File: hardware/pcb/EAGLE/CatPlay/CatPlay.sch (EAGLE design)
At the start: 5 parts

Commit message: updated pcb and gitignore
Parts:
- added Q1: 2N7002, CatPlay:2N7002
- added R1: (no value), rcl:R-US_R0603
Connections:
- new net N$1: Q1.D, R1.1
- net 5V: now also R1.2
- net L+: now also Q1.S
- net LSR: now also Q1.G
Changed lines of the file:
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@@
 <layers>
 <layer number="1" name="Top" color="4" fill="1" visible="no" active="no"/>
+<layer number="2" name="Route2" color="16" fill="1" visible="no" active="no"/>
+<layer number="3" name="Route3" color="17" fill="1" visible="no" active="no"/>
+<layer number="4" name="Route4" color="18" fill="1" visible="no" active="no"/>
+<layer number="5" name="Route5" color="19" fill="1" visible="no" active="no"/>
+<layer number="6" name="Route6" color="25" fill="1" visible="no" active="no"/>
+<layer number="7" name="Route7" color="26" fill="1" visible="no" active="no"/>
+<layer number="8" name="Route8" color="27" fill="1" visible="no" active="no"/>
+<layer number="9" name="Route9" color="28" fill="1" visible="no" active="no"/>
+<layer number="10" name="Route10" color="29" fill="1" visible="no" active="no"/>
+<layer number="11" name="Route11" color="30" fill="1" visible="no" active="no"/>
+<layer number="12" name="Route12" color="20" fill="1" visible="no" active="no"/>
+<layer number="13" name="Route13" color="21" fill="1" visible="no" active="no"/>
+<layer number="14" name="Route14" color="22" fill="1" visible="no" active="no"/>
+<layer number="15" name="Route15" color="23" fill="1" visible="no" active="no"/>
 <layer number="16" name="Bottom" color="1" fill="1" visible="no" active="no"/>
 <layer number="17" name="Pads" color="2" fill="1" visible="no" active="no"/>
@@
 <part name="GND3" library="supply1" library_urn="urn:adsk.eagle:library:371" deviceset="GND" device=""/>
 <part name="GND4" library="supply1" library_urn="urn:adsk.eagle:library:371" deviceset="GND" device=""/>
+<part name="Q1" library="CatPlay" deviceset="2N7002" device=""/>
+<part name="R1" library="rcl" library_urn="urn:adsk.eagle:library:334" deviceset="R-US_" device="R0603" package3d_urn="urn:adsk.eagle:package:23555/3"/>
 </parts>
 <sheets>
@@
 <attribute name="VALUE" x="27.94" y="35.56" size="1.778" layer="96"/>
 </instance>
+<instance part="Q1" gate="G$1" x="35.56" y="-17.78" smashed="yes">
+<attribute name="VALUE" x="24.13" y="-17.78" size="1.778" layer="96"/>
+<attribute name="NAME" x="24.13" y="-15.24" size="1.778" layer="95"/>
+</instance>
+<instance part="R1" gate="G$1" x="38.1" y="-2.54" smashed="yes" rot="R90">
+<attribute name="NAME" x="36.6014" y="-6.35" size="1.778" layer="95" rot="R90"/>
+<attribute name="VALUE" x="41.402" y="-6.35" size="1.778" layer="96" rot="R90"/>
+</instance>
 </instances>
 <busses>
@@
 <label x="-10.16" y="-7.62" size="1.27" layer="95" xref="yes"/>
 </segment>
+<segment>
+<pinref part="Q1" gate="G$1" pin="S"/>
+<wire x1="38.1" y1="-22.86" x2="38.1" y2="-25.4" width="0.1524" layer="91"/>
+<wire x1="38.1" y1="-25.4" x2="43.18" y2="-25.4" width="0.1524" layer="91"/>
+<label x="43.18" y="-25.4" size="1.27" layer="95" xref="yes"/>
+</segment>
 </net>
 <net name="5V" class="0">
@@
 <wire x1="38.1" y1="48.26" x2="25.4" y2="48.26" width="0.1524" layer="91"/>
 <label x="25.4" y="48.26" size="1.27" layer="95" rot="R180" xref="yes"/>
+</segment>
+<segment>
+<pinref part="R1" gate="G$1" pin="2"/>
+<wire x1="38.1" y1="2.54" x2="38.1" y2="5.08" width="0.1524" layer="91"/>
+<wire x1="38.1" y1="5.08" x2="27.94" y2="5.08" width="0.1524" layer="91"/>
+<label x="27.94" y="5.08" size="1.27" layer="95" rot="R180" xref="yes"/>
 </segment>
 </net>
@@
 <wire x1="30.48" y1="17.78" x2="25.4" y2="17.78" width="0.1524" layer="91"/>
 <label x="25.4" y="17.78" size="1.27" layer="95" rot="R180" xref="yes"/>
+</segment>
+<segment>
+<pinref part="Q1" gate="G$1" pin="G"/>
+<wire x1="33.02" y1="-20.32" x2="27.94" y2="-20.32" width="0.1524" layer="91"/>
+<label x="27.94" y="-20.32" size="1.27" layer="95" rot="R180" xref="yes"/>
+</segment>
+</net>
+<net name="N$1" class="0">
+<segment>
+<pinref part="Q1" gate="G$1" pin="D"/>
+<pinref part="R1" gate="G$1" pin="1"/>
+<wire x1="38.1" y1="-12.7" x2="38.1" y2="-7.62" width="0.1524" layer="91"/>
 </segment>
 </net>
@@
 packages will not be understood (or retained) with this version.
 </note>
+<note version="8.4" severity="warning">
+Since Version 8.4, EAGLE supports properties for SPICE simulation.
+Probes in schematics and SPICE mapping objects found in parts and library devices
+will not be understood with this version. Update EAGLE to the latest version
+for full support of SPICE simulation.
+</note>
 </compatibility>

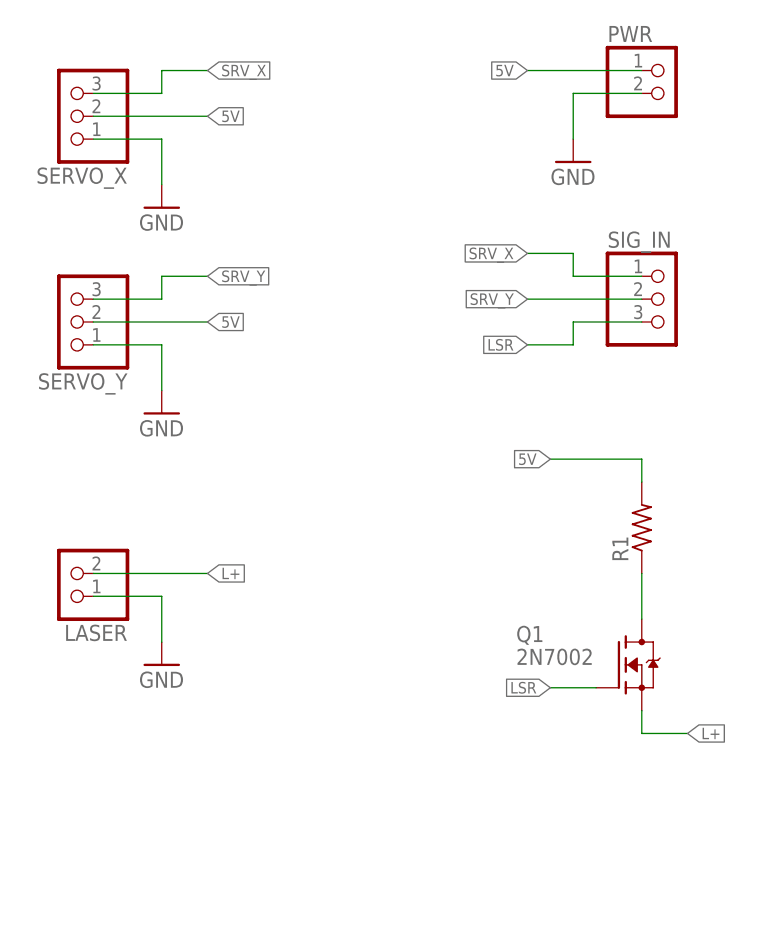
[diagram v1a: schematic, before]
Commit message: Updated Schematic [CAT-4]
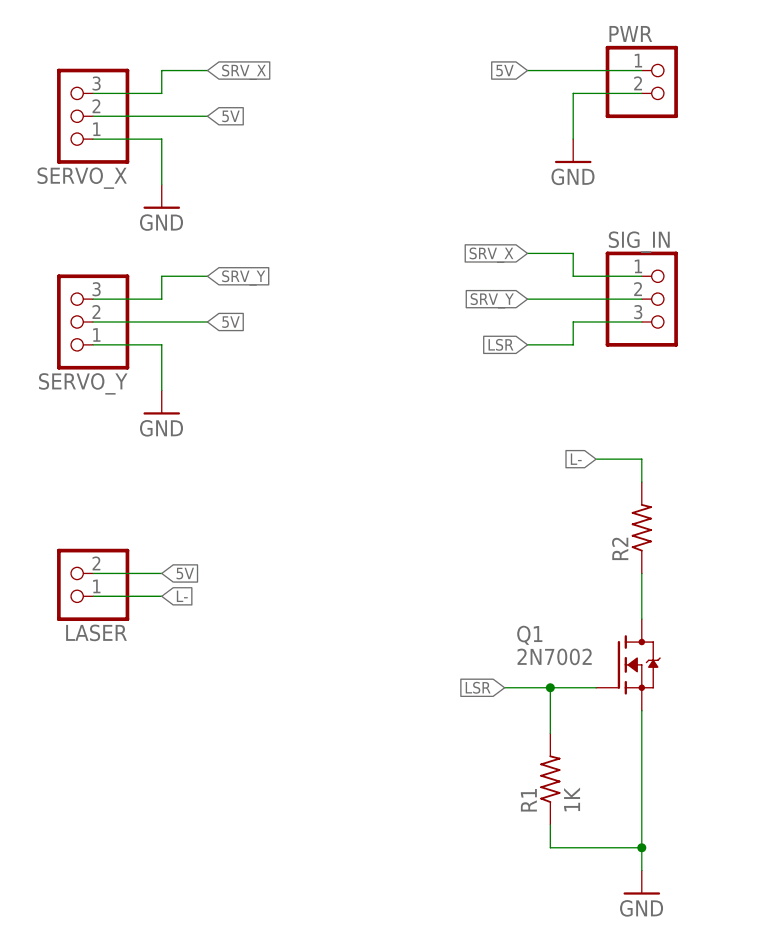
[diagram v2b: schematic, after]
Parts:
- added R2: (no value), rcl:R-US_R0603
- R1: value (none) -> 1K
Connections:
- removed net L+: LASER.2, Q1.S
- removed net N$1: Q1.D, R1.1
- new net L-: LASER.1, R2.2
- new net N$3: Q1.D, R2.1
- net 5V: now also LASER.2; no longer R1.2
- net GND: now also Q1.S, R1.1; no longer LASER.1
- net LSR: now also R1.2
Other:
- moved on the sheet: R1
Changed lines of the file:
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@@
 <part name="GND1" library="supply1" library_urn="urn:adsk.eagle:library:371" deviceset="GND" device=""/>
 <part name="GND2" library="supply1" library_urn="urn:adsk.eagle:library:371" deviceset="GND" device=""/>
-<part name="GND3" library="supply1" library_urn="urn:adsk.eagle:library:371" deviceset="GND" device=""/>
 <part name="GND4" library="supply1" library_urn="urn:adsk.eagle:library:371" deviceset="GND" device=""/>
 <part name="Q1" library="CatPlay" deviceset="2N7002" device=""/>
-<part name="R1" library="rcl" library_urn="urn:adsk.eagle:library:334" deviceset="R-US_" device="R0603" package3d_urn="urn:adsk.eagle:package:23555/3"/>
+<part name="R1" library="rcl" library_urn="urn:adsk.eagle:library:334" deviceset="R-US_" device="R0603" package3d_urn="urn:adsk.eagle:package:23555/3" value="1K"/>
+<part name="GND5" library="supply1" library_urn="urn:adsk.eagle:library:371" deviceset="GND" device=""/>
+<part name="R2" library="rcl" library_urn="urn:adsk.eagle:library:334" deviceset="R-US_" device="R0603" package3d_urn="urn:adsk.eagle:package:23555/3"/>
 </parts>
 <sheets>
@@
 <attribute name="VALUE" x="-17.78" y="30.48" size="1.778" layer="96"/>
 </instance>
-<instance part="GND3" gate="1" x="-15.24" y="-17.78" smashed="yes">
-<attribute name="VALUE" x="-17.78" y="-20.32" size="1.778" layer="96"/>
-</instance>
 <instance part="GND4" gate="1" x="30.48" y="38.1" smashed="yes">
 <attribute name="VALUE" x="27.94" y="35.56" size="1.778" layer="96"/>
@@
 <attribute name="NAME" x="24.13" y="-15.24" size="1.778" layer="95"/>
 </instance>
-<instance part="R1" gate="G$1" x="38.1" y="-2.54" smashed="yes" rot="R90">
+<instance part="R1" gate="G$1" x="27.94" y="-30.48" smashed="yes" rot="R90">
+<attribute name="NAME" x="26.4414" y="-34.29" size="1.778" layer="95" rot="R90"/>
+<attribute name="VALUE" x="31.242" y="-34.29" size="1.778" layer="96" rot="R90"/>
+</instance>
+<instance part="GND5" gate="1" x="38.1" y="-43.18" smashed="yes">
+<attribute name="VALUE" x="35.56" y="-45.72" size="1.778" layer="96"/>
+</instance>
+<instance part="R2" gate="G$1" x="38.1" y="-2.54" smashed="yes" rot="R90">
 <attribute name="NAME" x="36.6014" y="-6.35" size="1.778" layer="95" rot="R90"/>
 <attribute name="VALUE" x="41.402" y="-6.35" size="1.778" layer="96" rot="R90"/>
@@
 </segment>
 <segment>
-<pinref part="LASER" gate="G$1" pin="1"/>
-<pinref part="GND3" gate="1" pin="GND"/>
-<wire x1="-22.86" y1="-10.16" x2="-15.24" y2="-10.16" width="0.1524" layer="91"/>
-<wire x1="-15.24" y1="-10.16" x2="-15.24" y2="-15.24" width="0.1524" layer="91"/>
-</segment>
-<segment>
 <pinref part="GND4" gate="1" pin="GND"/>
 <pinref part="PWR" gate="G$1" pin="2"/>
@@
 <wire x1="30.48" y1="45.72" x2="38.1" y2="45.72" width="0.1524" layer="91"/>
 </segment>
-</net>
-<net name="L+" class="0">
-<segment>
-<pinref part="LASER" gate="G$1" pin="2"/>
-<wire x1="-22.86" y1="-7.62" x2="-10.16" y2="-7.62" width="0.1524" layer="91"/>
-<label x="-10.16" y="-7.62" size="1.27" layer="95" xref="yes"/>
-</segment>
 <segment>
 <pinref part="Q1" gate="G$1" pin="S"/>
-<wire x1="38.1" y1="-22.86" x2="38.1" y2="-25.4" width="0.1524" layer="91"/>
-<wire x1="38.1" y1="-25.4" x2="43.18" y2="-25.4" width="0.1524" layer="91"/>
-<label x="43.18" y="-25.4" size="1.27" layer="95" xref="yes"/>
+<wire x1="38.1" y1="-22.86" x2="38.1" y2="-38.1" width="0.1524" layer="91"/>
+<pinref part="R1" gate="G$1" pin="1"/>
+<wire x1="38.1" y1="-38.1" x2="27.94" y2="-38.1" width="0.1524" layer="91"/>
+<wire x1="27.94" y1="-38.1" x2="27.94" y2="-35.56" width="0.1524" layer="91"/>
+<wire x1="38.1" y1="-38.1" x2="38.1" y2="-40.64" width="0.1524" layer="91"/>
+<junction x="38.1" y="-38.1"/>
+<pinref part="GND5" gate="1" pin="GND"/>
 </segment>
 </net>
@@
 </segment>
 <segment>
-<pinref part="R1" gate="G$1" pin="2"/>
-<wire x1="38.1" y1="2.54" x2="38.1" y2="5.08" width="0.1524" layer="91"/>
-<wire x1="38.1" y1="5.08" x2="27.94" y2="5.08" width="0.1524" layer="91"/>
-<label x="27.94" y="5.08" size="1.27" layer="95" rot="R180" xref="yes"/>
+<pinref part="LASER" gate="G$1" pin="2"/>
+<wire x1="-22.86" y1="-7.62" x2="-15.24" y2="-7.62" width="0.1524" layer="91"/>
+<label x="-15.24" y="-7.62" size="1.27" layer="95" xref="yes"/>
 </segment>
 </net>
@@
 <segment>
 <pinref part="Q1" gate="G$1" pin="G"/>
+<pinref part="R1" gate="G$1" pin="2"/>
 <wire x1="33.02" y1="-20.32" x2="27.94" y2="-20.32" width="0.1524" layer="91"/>
-<label x="27.94" y="-20.32" size="1.27" layer="95" rot="R180" xref="yes"/>
+<wire x1="27.94" y1="-20.32" x2="27.94" y2="-25.4" width="0.1524" layer="91"/>
+<wire x1="27.94" y1="-20.32" x2="22.86" y2="-20.32" width="0.1524" layer="91"/>
+<junction x="27.94" y="-20.32"/>
+<label x="22.86" y="-20.32" size="1.27" layer="95" rot="R180" xref="yes"/>
 </segment>
 </net>
-<net name="N$1" class="0">
+<net name="N$3" class="0">
 <segment>
 <pinref part="Q1" gate="G$1" pin="D"/>
-<pinref part="R1" gate="G$1" pin="1"/>
+<pinref part="R2" gate="G$1" pin="1"/>
 <wire x1="38.1" y1="-12.7" x2="38.1" y2="-7.62" width="0.1524" layer="91"/>
 </segment>
 </net>
+<net name="L-" class="0">
+<segment>
+<pinref part="R2" gate="G$1" pin="2"/>
+<wire x1="38.1" y1="2.54" x2="38.1" y2="5.08" width="0.1524" layer="91"/>
+<wire x1="38.1" y1="5.08" x2="33.02" y2="5.08" width="0.1524" layer="91"/>
+<label x="33.02" y="5.08" size="1.27" layer="95" rot="R180" xref="yes"/>
+</segment>
+<segment>
+<pinref part="LASER" gate="G$1" pin="1"/>
+<wire x1="-22.86" y1="-10.16" x2="-15.24" y2="-10.16" width="0.1524" layer="91"/>
+<label x="-15.24" y="-10.16" size="1.27" layer="95" xref="yes"/>
+</segment>
+</net>
